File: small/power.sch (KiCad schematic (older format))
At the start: 28 parts, among them J2 Screw_Terminal_01x02, U10 TPS5430DDAR, U2 LM7805_TO220, U20 TPS5430DDAR

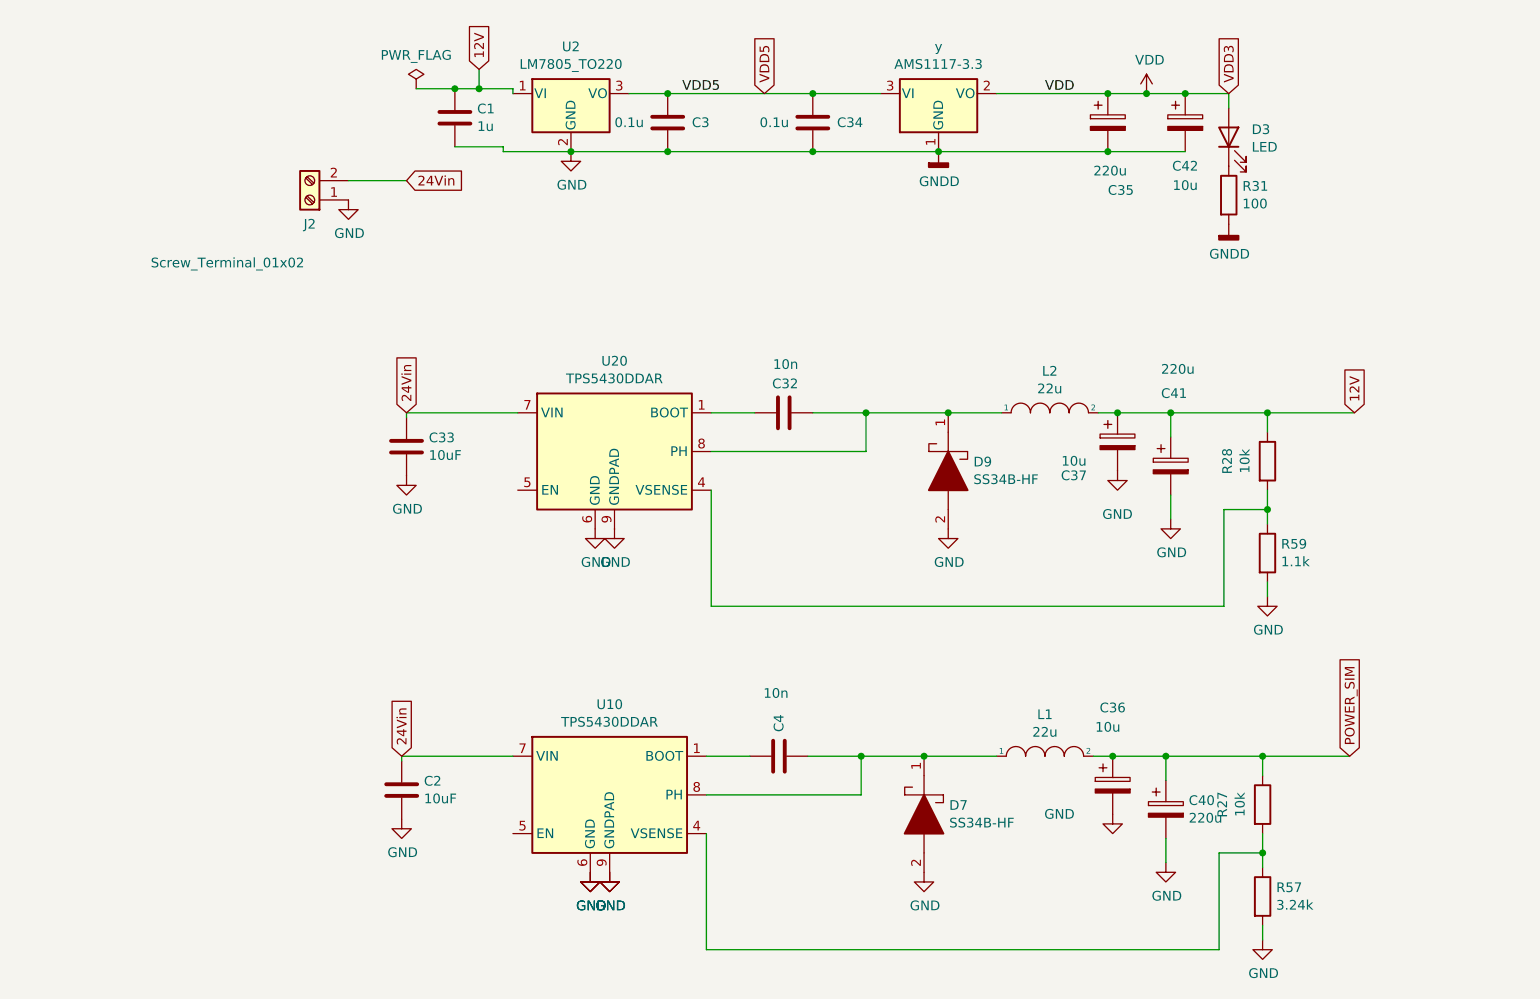
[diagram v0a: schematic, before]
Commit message: Isolated DCDC added
power LED added
reverse voltage protection added
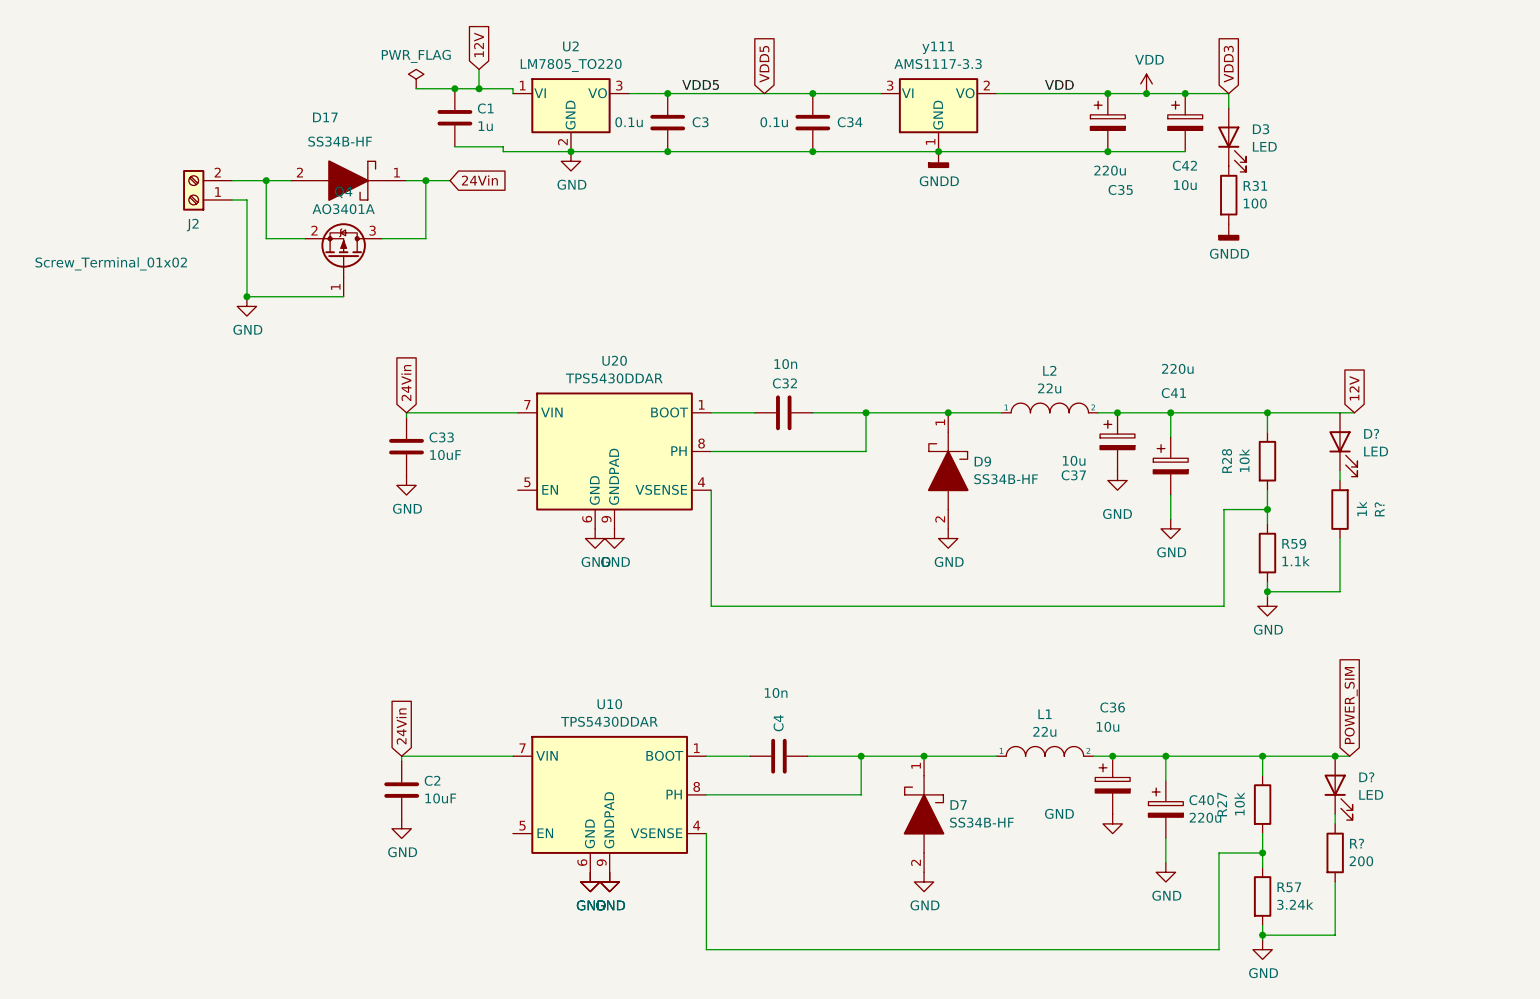
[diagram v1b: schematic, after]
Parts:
- added D17: SS34B-HF, mylib:DIOM5336X320N, symbol saxli-rescue:SS34B-HF-ss34
- added D? (x2): LED, LED_SMD:LED_0805_2012Metric_Pad1.15x1.40mm_HandSolder, symbol Device:LED
- added Q4: AO3401A, Package_TO_SOT_SMD:SOT-23, symbol Transistor_FET:AO3401A
- added R?: 200, Resistor_SMD:R_0603_1608Metric, symbol Device:R
- added R?: 1k, Resistor_SMD:R_0805_2012Metric, symbol Device:R
- renumbered у to у111
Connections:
- net 24Vin: now also D17.1, Q4.3 (D); no longer J2.2 (Pin_2)
- net GND: now also Q4.1 (G), R?.1, R?.2
- net POWER_SIM: now also D?.2 (A)
- new net: D17.2, J2.2 (Pin_2), Q4.2 (S)
- new net: D?.1 (K), R?.1
- new net: D?.1 (K), R?.2
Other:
- moved on the sheet: J2
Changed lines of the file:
@@
 $EndComp
 Wire Wire Line
-	7275 3450 7275 3525
+	7275 3450 7275 3500
 Connection ~ 7275 2575
 Wire Wire Line
@@
 $EndComp
 Wire Wire Line
-	7250 5225 7250 5300
+	7250 5225 7250 5275
 Connection ~ 7250 4350
 Wire Wire Line
@@
 	7275 2575 7725 2575
 $Comp
-L Regulator_Linear:LD1117S33TR_SOT223 у
+L Regulator_Linear:LD1117S33TR_SOT223 у111
 U 1 1 607A31DD
 P 5575 925
-F 0 "у" H 5575 1167 50  0000 C CNN
+F 0 "у111" H 5575 1167 50  0000 C CNN
 F 1 "AMS1117-3.3" H 5575 1076 50  0000 C CNN
 F 2 "Package_TO_SOT_SMD:SOT-223" H 5575 1125 50  0001 C CNN
@@
 Text GLabel 3200 800  1    50   Input ~ 0
 12V
-$Comp
-L Connector:Screw_Terminal_01x02 J2
-U 1 1 607A3252
-P 2325 1475
-F 0 "J2" H 2325 1600 50  0000 C CNN
-F 1 "Screw_Terminal_01x02" H 2750 1800 50  0000 C CNN
-F 2 "TerminalBlock_Phoenix:TerminalBlock_Phoenix_MKDS-1,5-2-5.08_1x02_P5.08mm_Horizontal" H 2325 1475 50  0001 C CNN
-F 3 "~" H 2325 1475 50  0001 C CNN
-F 4 "Connector unknown" H 2325 1475 50  0001 C CNN "Mpn"
-F 5 "N/A" H 2325 1475 50  0001 C CNN "LCSC"
-	1    2325 1475
-	-1   0    0    1
-$EndComp
-$Comp
-L power:GND #PWR01
-U 1 1 607A3258
-P 2525 1475
-F 0 "#PWR01" H 2525 1225 50  0001 C CNN
-F 1 "GND" H 2530 1302 50  0000 C CNN
-F 2 "" H 2525 1475 50  0001 C CNN
-F 3 "" H 2525 1475 50  0001 C CNN
-	1    2525 1475
-	1    0    0    -1
-$EndComp
-Wire Wire Line
-	2525 1375 2825 1375
-Text GLabel 2825 1375 2    50   Input ~ 0
+Wire Wire Line
+	1925 1375 2100 1375
+Text GLabel 3050 1375 2    50   Input ~ 0
 24Vin
 $Comp
@@
 	1    0    0    -1
 $EndComp
-Wire Wire Line
-	7250 4350 7700 4350
 $Comp
 L Device:LED D?
@@
 	1    0    0    -1
 $EndComp
+$Comp
+L saxli-rescue:SS34B-HF-ss34 D17
+U 1 1 603B2147
+P 2925 1375
+F 0 "D17" H 3375 1050 50  0000 L CNN
+F 1 "SS34B-HF" H 3200 1175 50  0000 L CNN
+F 2 "mylib:DIOM5336X320N" H 3425 1525 50  0001 L CNN
+F 3 "https://www.mouser.jp/datasheet/2/80/SP-JB017_SS34B-HF_Thru._SS320B-HF_RevB-1847021.pdf" H 3425 1425 50  0001 L CNN
+F 4 "Schottky Diodes & Rectifiers DIODE SCHOTTKY 3A 40V SMB" H 3425 1325 50  0001 L CNN "Description"
+F 5 "3.2" H 3425 1225 50  0001 L CNN "Height"
+F 6 "" H 3425 1125 50  0001 L CNN "Manufacturer_Name"
+F 7 "" H 3425 1025 50  0001 L CNN "Manufacturer_Part_Number"
+F 8 "750-SS34B-HF" H 3425 925 50  0001 L CNN "Mouser Part Number"
+F 9 "https://www.mouser.co.uk/ProductDetail/Comchip-Technology/SS34B-HF/?qs=vmHwEFxEFR9G1M%252BcUPG%2FxQ%3D%3D" H 3425 825 50  0001 L CNN "Mouser Price/Stock"
+F 10 "" H 3425 725 50  0001 L CNN "Arrow Part Number"
+F 11 "" H 3425 625 50  0001 L CNN "Arrow Price/Stock"
+F 12 "C8678" H 2925 1375 50  0001 C CNN "LCSC"
+F 13 "SS34B-HF" H 2925 1375 50  0001 C CNN "MPN"
+F 14 "0.0350" H 2925 1375 50  0001 C CNN "Price"
+F 15 "0" H 2925 1375 50  0001 C CNN "source"
+	1    2925 1375
+	-1   0    0    1
+$EndComp
+$Comp
+L Transistor_FET:AO3401A Q4
+U 1 1 603B5293
+P 2500 1775
+F 0 "Q4" V 2842 1775 50  0000 C CNN
+F 1 "AO3401A" V 2751 1775 50  0000 C CNN
+F 2 "Package_TO_SOT_SMD:SOT-23" H 2700 1700 50  0001 L CIN
+F 3 "https://datasheet.lcsc.com/szlcsc/Alpha-Omega-Semicon-AOS-AO3401A_C15127.pdf" H 2500 1775 50  0001 L CNN
+F 4 "C15127" V 2500 1775 50  0001 C CNN "LCSC"
+F 5 "0.1023" V 2500 1775 50  0001 C CNN "Price"
+F 6 "AO3401A" V 2500 1775 50  0001 C CNN "MPN"
+	1    2500 1775
+	0    1    -1   0
+$EndComp
+Wire Wire Line
+	3050 1375 2925 1375
+Wire Wire Line
+	2925 1375 2925 1675
+Wire Wire Line
+	2925 1675 2700 1675
+Connection ~ 2925 1375
+Wire Wire Line
+	2925 1375 2825 1375
+Wire Wire Line
+	2300 1675 2100 1675
+Wire Wire Line
+	2100 1675 2100 1375
+Connection ~ 2100 1375
+Wire Wire Line
+	2100 1375 2225 1375
+$Comp
+L power:GND #PWR01
+U 1 1 607A3258
+P 2000 1975
+F 0 "#PWR01" H 2000 1725 50  0001 C CNN
+F 1 "GND" H 2005 1802 50  0000 C CNN
+F 2 "" H 2000 1975 50  0001 C CNN
+F 3 "" H 2000 1975 50  0001 C CNN
+	1    2000 1975
+	1    0    0    -1
+$EndComp
+$Comp
+L Connector:Screw_Terminal_01x02 J2
+U 1 1 607A3252
+P 1725 1475
+F 0 "J2" H 1725 1600 50  0000 C CNN
+F 1 "Screw_Terminal_01x02" H 2150 1800 50  0000 C CNN
+F 2 "TerminalBlock_Phoenix:TerminalBlock_Phoenix_MKDS-1,5-2-5.08_1x02_P5.08mm_Horizontal" H 1725 1475 50  0001 C CNN
+F 3 "~" H 1725 1475 50  0001 C CNN
+F 4 "Connector unknown" H 1725 1475 50  0001 C CNN "Mpn"
+F 5 "N/A" H 1725 1475 50  0001 C CNN "LCSC"
+	1    1725 1475
+	-1   0    0    1
+$EndComp
+Wire Wire Line
+	2500 1975 2000 1975
+Wire Wire Line
+	2000 1975 2000 1475
+Wire Wire Line
+	2000 1475 1925 1475
+Connection ~ 2000 1975
+$Comp
+L Device:LED D?
+U 1 1 603EF19F
+P 7625 4500
+AR Path="/602125D9/603EF19F" Ref="D?"  Part="1"
+AR Path="/6010B004/603EF19F" Ref="D?"  Part="1"
+F 0 "D?" V 7664 4382 50  0000 R CNN
+F 1 "LED" V 7573 4382 50  0000 R CNN
+F 2 "LED_SMD:LED_0805_2012Metric_Pad1.15x1.40mm_HandSolder" H 7625 4500 50  0001 C CNN
+F 3 "https://datasheet.lcsc.com/szlcsc/Foshan-NationStar-Optoelectronics-FC-2012HRK-620D_C84256.pdf" H 7625 4500 50  0001 C CNN
+F 4 "C205449" V 7625 4500 50  0001 C CNN "LCSC"
+F 5 "ORH-YG35A" H 7625 4500 50  0001 C CNN "MPN"
+F 6 "0.0093" H 7625 4500 50  0001 C CNN "Price"
+	1    7625 4500
+	0    -1   -1   0
+$EndComp
+$Comp
+L Device:R R?
+U 1 1 603EF1A9
+P 7625 4850
+AR Path="/602125D9/603EF1A9" Ref="R?"  Part="1"
+AR Path="/6010B004/603EF1A9" Ref="R?"  Part="1"
+F 0 "R?" H 7695 4896 50  0000 L CNN
+F 1 "200" H 7695 4805 50  0000 L CNN
+F 2 "Resistor_SMD:R_0603_1608Metric" V 7555 4850 50  0001 C CNN
+F 3 "https://datasheet.lcsc.com/szlcsc/Uniroyal-Elec-0603WAF2000T5E_C8218.pdf" H 7625 4850 50  0001 C CNN
+F 4 "C8218" H 7625 4850 50  0001 C CNN "LCSC"
+F 5 "0603WAF2000T5E" H 7625 4850 50  0001 C CNN "MPN"
+F 6 "0.0022" H 7625 4850 50  0001 C CNN "Price"
+F 7 "0" H 7625 4850 50  0001 C CNN "source"
+	1    7625 4850
+	1    0    0    -1
+$EndComp
+Wire Wire Line
+	7625 4650 7625 4700
+Wire Wire Line
+	7250 5275 7625 5275
+Wire Wire Line
+	7625 5275 7625 5000
+Connection ~ 7250 5275
+Wire Wire Line
+	7250 5275 7250 5300
+Wire Wire Line
+	7250 4350 7625 4350
+Connection ~ 7625 4350
+Wire Wire Line
+	7625 4350 7700 4350
+$Comp
+L Device:LED D?
+U 1 1 603F539D
+P 7650 2725
+AR Path="/602125D9/603F539D" Ref="D?"  Part="1"
+AR Path="/6010B004/603F539D" Ref="D?"  Part="1"
+F 0 "D?" V 7689 2607 50  0000 R CNN
+F 1 "LED" V 7598 2607 50  0000 R CNN
+F 2 "LED_SMD:LED_0805_2012Metric_Pad1.15x1.40mm_HandSolder" H 7650 2725 50  0001 C CNN
+F 3 "https://datasheet.lcsc.com/szlcsc/Foshan-NationStar-Optoelectronics-FC-2012HRK-620D_C84256.pdf" H 7650 2725 50  0001 C CNN
+F 4 "C205449" V 7650 2725 50  0001 C CNN "LCSC"
+F 5 "ORH-YG35A" H 7650 2725 50  0001 C CNN "MPN"
+F 6 "0.0093" H 7650 2725 50  0001 C CNN "Price"
+	1    7650 2725
+	0    -1   -1   0
+$EndComp
+Wire Wire Line
+	7650 2875 7650 2925
+$Comp
+L Device:R R?
+U 1 1 603FCE65
+P 7650 3075
+AR Path="/603FCE65" Ref="R?"  Part="1"
+AR Path="/652E8962/603FCE65" Ref="R?"  Part="1"
+F 0 "R?" V 7443 3075 50  0000 C CNN
+F 1 "1k" V 7534 3075 50  0000 C CNN
+F 2 "Resistor_SMD:R_0805_2012Metric" V 7580 3075 50  0001 C CNN
+F 3 "https://datasheet.lcsc.com/szlcsc/Uniroyal-Elec-0805W8F1001T5E_C17513.pdf" H 7650 3075 50  0001 C CNN
+F 4 "C17513" V 7650 3075 50  0001 C CNN "LCSC"
+F 5 "0.0040" V 7650 3075 50  0001 C CNN "Price"
+F 6 "0805W8F1001T5E" H 7650 3075 50  0001 C CNN "MPN"
+F 7 "0" H 7650 3075 50  0001 C CNN "source"
+	1    7650 3075
+	-1   0    0    1
+$EndComp
+Wire Wire Line
+	7275 3500 7650 3500
+Wire Wire Line
+	7650 3500 7650 3225
+Connection ~ 7275 3500
+Wire Wire Line
+	7275 3500 7275 3525
 $EndSCHEMATC

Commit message: fabrication output prepared
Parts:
- gave numbers to parts that had none: 4
- renumbered у111 to у1111
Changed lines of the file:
@@
 	7275 2575 7725 2575
 $Comp
-L Regulator_Linear:LD1117S33TR_SOT223 у111
+L Regulator_Linear:LD1117S33TR_SOT223 у1111
 U 1 1 607A31DD
 P 5575 925
-F 0 "у111" H 5575 1167 50  0000 C CNN
+F 0 "у1111" H 5575 1167 50  0000 C CNN
 F 1 "AMS1117-3.3" H 5575 1076 50  0000 C CNN
 F 2 "Package_TO_SOT_SMD:SOT-223" H 5575 1125 50  0001 C CNN
@@
 P 7625 4500
 AR Path="/602125D9/603EF19F" Ref="D?"  Part="1"
-AR Path="/6010B004/603EF19F" Ref="D?"  Part="1"
-F 0 "D?" V 7664 4382 50  0000 R CNN
+AR Path="/6010B004/603EF19F" Ref="D18"  Part="1"
+F 0 "D18" V 7664 4382 50  0000 R CNN
 F 1 "LED" V 7573 4382 50  0000 R CNN
 F 2 "LED_SMD:LED_0805_2012Metric_Pad1.15x1.40mm_HandSolder" H 7625 4500 50  0001 C CNN
@@
 P 7625 4850
 AR Path="/602125D9/603EF1A9" Ref="R?"  Part="1"
-AR Path="/6010B004/603EF1A9" Ref="R?"  Part="1"
-F 0 "R?" H 7695 4896 50  0000 L CNN
+AR Path="/6010B004/603EF1A9" Ref="R52"  Part="1"
+F 0 "R52" H 7695 4896 50  0000 L CNN
 F 1 "200" H 7695 4805 50  0000 L CNN
 F 2 "Resistor_SMD:R_0603_1608Metric" V 7555 4850 50  0001 C CNN
@@
 P 7650 2725
 AR Path="/602125D9/603F539D" Ref="D?"  Part="1"
-AR Path="/6010B004/603F539D" Ref="D?"  Part="1"
-F 0 "D?" V 7689 2607 50  0000 R CNN
+AR Path="/6010B004/603F539D" Ref="D19"  Part="1"
+F 0 "D19" V 7689 2607 50  0000 R CNN
 F 1 "LED" V 7598 2607 50  0000 R CNN
 F 2 "LED_SMD:LED_0805_2012Metric_Pad1.15x1.40mm_HandSolder" H 7650 2725 50  0001 C CNN
@@
 AR Path="/603FCE65" Ref="R?"  Part="1"
 AR Path="/652E8962/603FCE65" Ref="R?"  Part="1"
-F 0 "R?" V 7443 3075 50  0000 C CNN
+AR Path="/6010B004/603FCE65" Ref="R53"  Part="1"
+F 0 "R53" V 7443 3075 50  0000 C CNN
 F 1 "1k" V 7534 3075 50  0000 C CNN
 F 2 "Resistor_SMD:R_0805_2012Metric" V 7580 3075 50  0001 C CNN

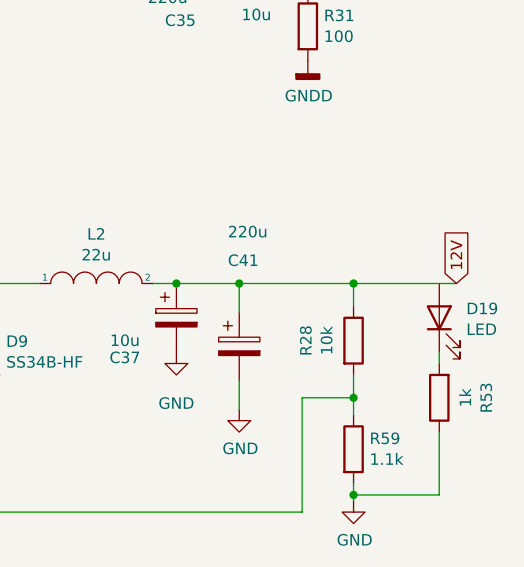
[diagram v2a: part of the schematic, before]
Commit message: working on JLCPCB orientations
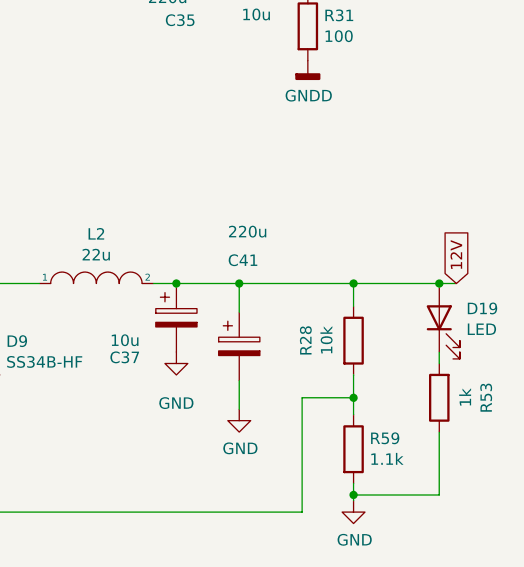
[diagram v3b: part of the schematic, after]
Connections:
- net 12V: now also D19.2 (A)

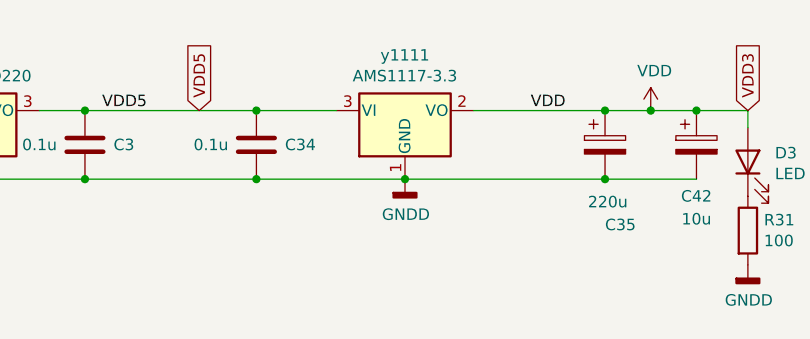
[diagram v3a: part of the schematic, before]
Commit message: oscillator footprint and capacitors changed
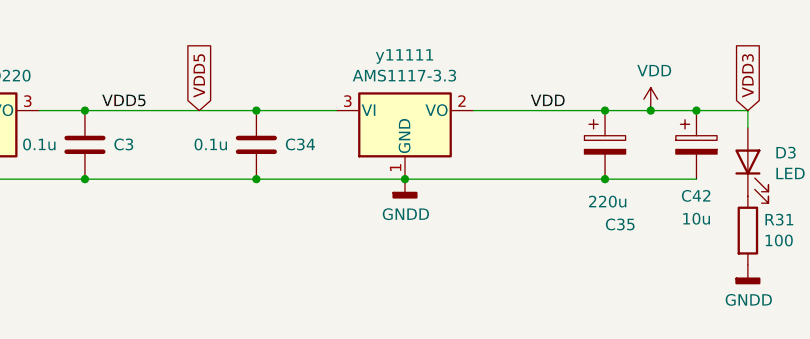
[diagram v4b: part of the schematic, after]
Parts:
- renumbered у1111 to у11111
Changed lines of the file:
@@
 24Vin
 $Comp
-L Regulator_Linear:LD1117S33TR_SOT223 у1111
+L Regulator_Linear:LD1117S33TR_SOT223 у11111
 U 1 1 607A31DD
 P 5575 925
-F 0 "у1111" H 5575 1167 50  0000 C CNN
+F 0 "у11111" H 5575 1167 50  0000 C CNN
 F 1 "AMS1117-3.3" H 5575 1076 50  0000 C CNN
 F 2 "Package_TO_SOT_SMD:SOT-223" H 5575 1125 50  0001 C CNN

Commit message: iso voltage update
minor changes
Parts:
- renumbered у11111 to U3
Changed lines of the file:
@@
 24Vin
 $Comp
-L Regulator_Linear:LD1117S33TR_SOT223 у11111
+L Regulator_Linear:LD1117S33TR_SOT223 U3
 U 1 1 607A31DD
 P 5575 925
-F 0 "у11111" H 5575 1167 50  0000 C CNN
+F 0 "U3" H 5575 1167 50  0000 C CNN
 F 1 "AMS1117-3.3" H 5575 1076 50  0000 C CNN
 F 2 "Package_TO_SOT_SMD:SOT-223" H 5575 1125 50  0001 C CNN
